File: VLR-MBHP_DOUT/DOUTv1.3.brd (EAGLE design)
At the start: 59.8 x 140 mm, 20 parts, among them IC2 74HC595, IC3 74HC595, IC4 74HC595

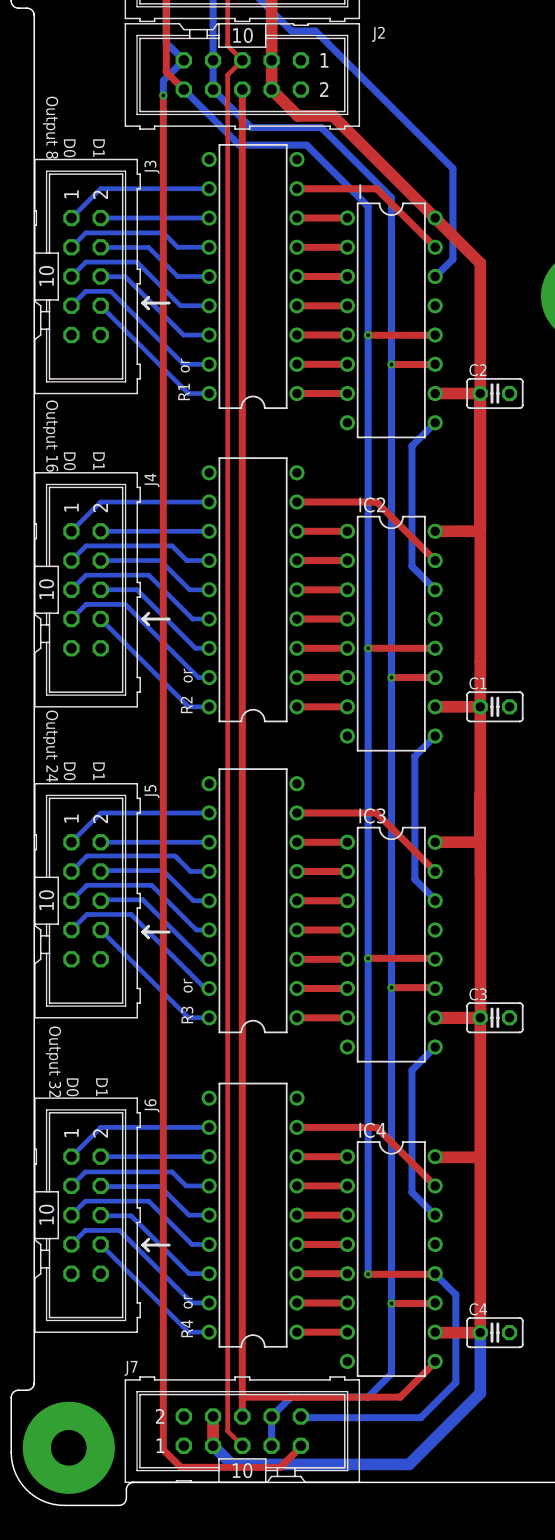
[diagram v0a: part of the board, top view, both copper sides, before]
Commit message: D IN/OUT changes
Didn’t get it to a second prototype jet but because of the changes
related to the first prototype im quite shure this works.
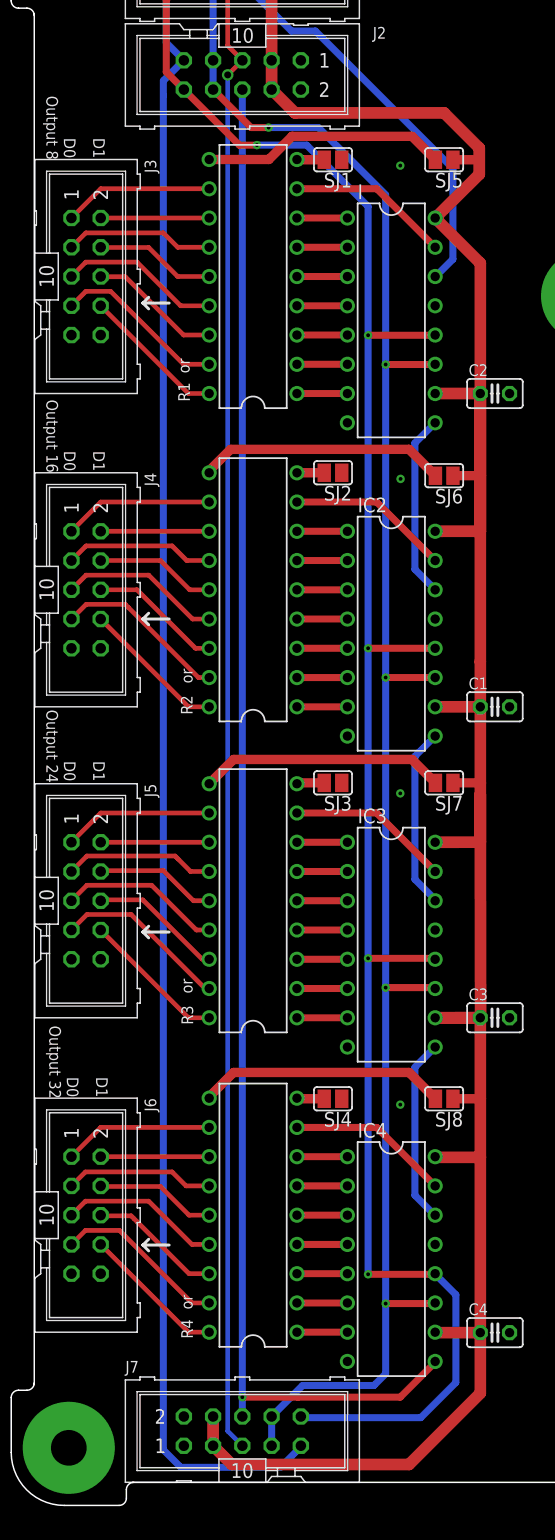
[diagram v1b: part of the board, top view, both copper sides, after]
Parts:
- added SJ1, SJ2, SJ3, SJ4, SJ5, SJ6, SJ7, SJ8: (no value), Jumper:SJ
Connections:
- new net N$74: R1.9, SJ1.2
- new net N$75: R1.10, SJ5.2
- new net N$76: R2.10, SJ6.2
- new net N$77: R2.9, SJ2.2
- new net N$78: R3.9, SJ3.2
- new net N$79: R3.10, SJ7.2
- new net N$80: R4.10, SJ8.2
- new net N$81: R4.9, SJ4.2
- net +5V: now also SJ5.1, SJ6.1, SJ7.1, SJ8.1
- net GND: now also SJ1.1, SJ2.1, SJ3.1, SJ4.1; no longer R1.9, R2.9, R3.9, R4.9
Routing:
- net N$80: track 0.00 -> 21.6 mm
- net N$76: track 0.00 -> 21.5 mm
- net N$79: track 0.00 -> 21.4 mm
- net N$75: track 0.00 -> 21.3 mm
- net +5V: track 210.8 -> 229.3 mm
- net N$78: track 0.00 -> 2.40 mm
- net N$81: track 0.00 -> 2.39 mm
- net N$74: track 0.00 -> 2.38 mm
- net N$77: track 0.00 -> 2.37 mm
- net N$71: track 163.1 -> 164.3 mm, vias 4 -> 5
- net N$72: vias 4 -> 5
- net N$70: vias 0 -> 2
- net N$65: vias 0 -> 1
- net N$38: vias 0 -> 1
- net N$36: vias 0 -> 1
